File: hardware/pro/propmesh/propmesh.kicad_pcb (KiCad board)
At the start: 2 copper layers, 154 parts, among them CN1 LINE_OUT, J1 DC_IN, J10 SERVO, J11 SERVO, J12 SERVO, J13 SERVO, J15 MS_SEL, J16 DIAG_AUX, J19 MS_SEL, J2 DC_JACK, J20 MS_SEL, J21 MS_SEL, J22 MS_SEL, J23 MS_SEL, J24 DIAG_AUX, J3 RELAY_OUT, J4 TYPE-C-31-M-12, J5 SPEAKER, J6 RELAY_OUT, J7 SERVO, J8 RELAY_OUT, J9 SERVO, K1 HK4100F-DC5V-SHG, K2 HK4100F-DC5V-SHG, K3 HK4100F-DC5V-SHG, Q1 AO3400A, Q2 AOD4185, Q3 AO3400A, Q4 AO3400A, Q5 AO3400A, Q6 AO3400A, Q7 AO3400A, Q8 AO3400A, SW1 TS-1187A, SW2 TS-1187A, U1 TLV62569DBV, U2 AP64350SP-13, U3 ESP32-S3-WROOM-1U-N8R2, U4 USBLC6-2SC6, U5 PCA9685PW, U6 ULN2003A, U7 MAX98357AETE+T, U8 PCM5102APWR

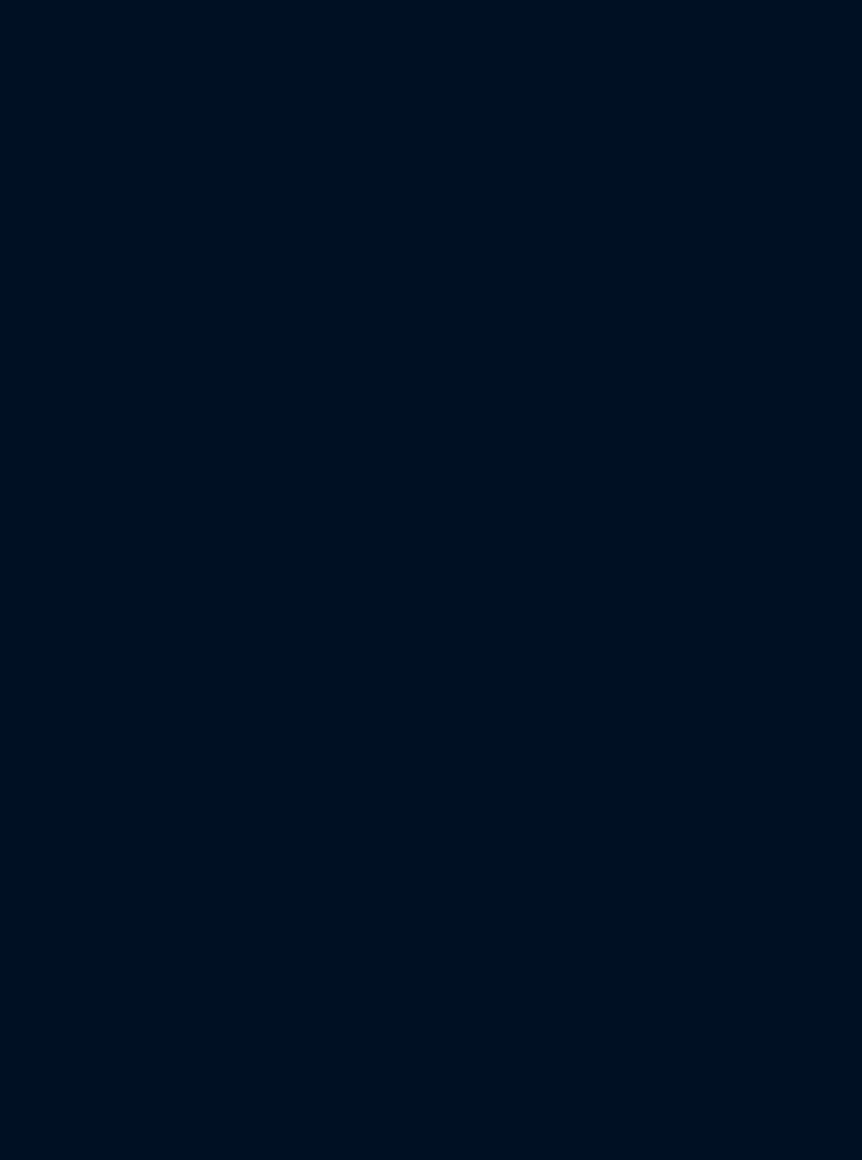
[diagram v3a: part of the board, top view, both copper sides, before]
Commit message: Sheet 07 (sensors + expansion) captured; sheet 05 spec ready
Sheet 07 drawn and verified: 3 clamped digital inputs (+ PIR header),
2 halved analog inputs, TSOP38238 on filtered 3V3, Qwiic (SH-1.0 clone
C7430446 — genuine JST stock-dead), 2x5 expansion header with GPIO45/46
strap protection. checknet all green, ERC clean bar the 4 LED labels
awaiting sheet 05. D2_MID global on motors + sensors sheets so
expansion pin 9 rides GPIO43's 1k.

Sheet 05 spec: AHCT125 moved to SOIC-14 C155176 (TSSOP dead at JLC),
strip 2 = 2x DG128-02P (04P dead), WS2812B-MINI-X2 status pixel
imported + datasheet-verified (pins, land pattern, VIH math).

Cost: all seven blocks now verified; parts subtotal $31.93,
duty-paid ~$48.55. Open item #2 mostly resolved (residual: JLC order
UI check before first PCBA run).

New repo rule after the C_A1 collision: spec refs are project-global —
never reuse one across sheet yamls (audio R_D3 -> R_DAT3, sensor caps
-> C_AN1/2).

Co-Authored-By: Claude Fable 5 <noreply@anthropic.com>
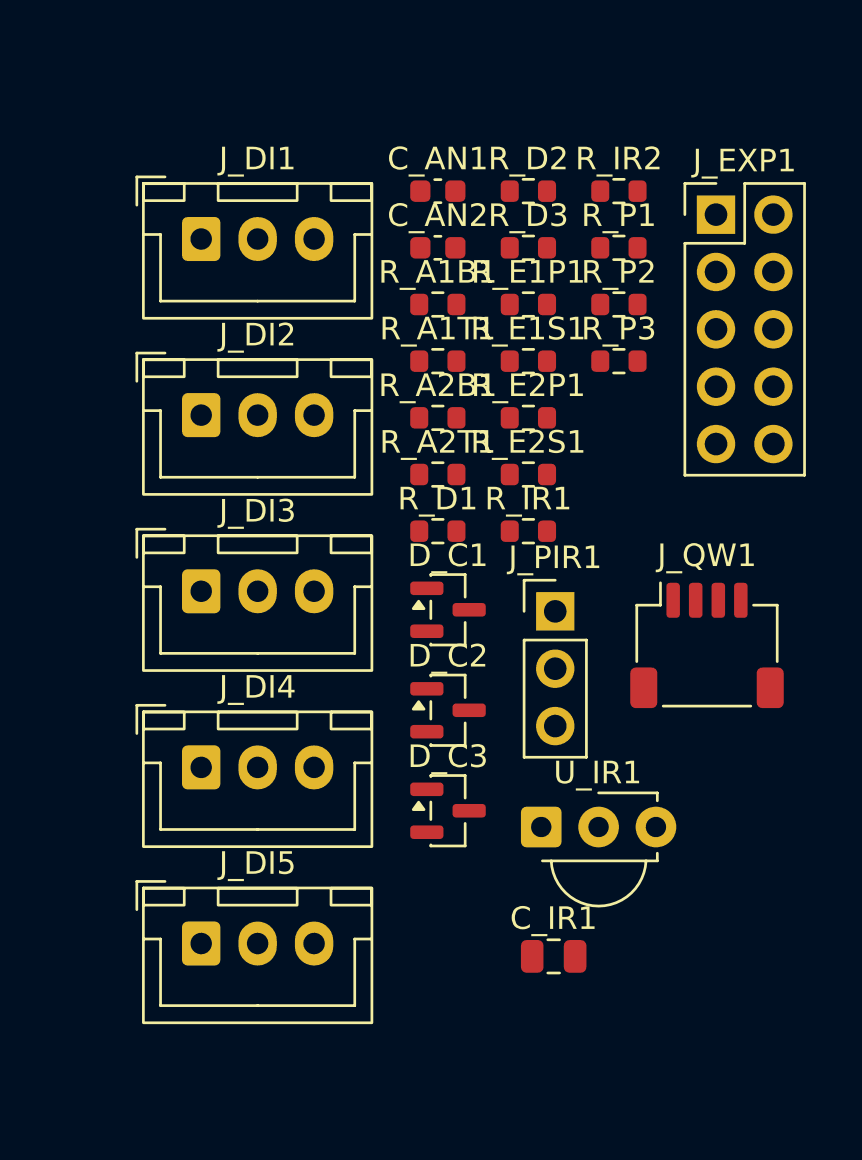
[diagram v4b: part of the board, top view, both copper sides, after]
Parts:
- added C_AN1: 100n, Capacitor_SMD:C_0603_1608Metric, F.Cu at (244.5, 23.8)
- added C_AN2: 100n, Capacitor_SMD:C_0603_1608Metric, F.Cu at (244.5, 26.3)
- added C_IR1: 10u, Capacitor_SMD:C_0805_2012Metric, F.Cu at (249.6, 57.6)
- added D_C1: BAT54S, Package_TO_SOT_SMD:SOT-23, F.Cu at (244.9, 42.3)
- added D_C2: BAT54S, Package_TO_SOT_SMD:SOT-23, F.Cu at (244.9, 46.7)
- added D_C3: BAT54S, Package_TO_SOT_SMD:SOT-23, F.Cu at (244.9, 51.2)
- added J_DI1: DIG_IN, Connector_JST:JST_XH_B3B-XH-A_1x03_P2.50mm_Vertical, F.Cu at (234.0, 25.9)
- added J_DI2: DIG_IN, Connector_JST:JST_XH_B3B-XH-A_1x03_P2.50mm_Vertical, F.Cu at (234.0, 33.7)
- added J_DI3: DIG_IN, Connector_JST:JST_XH_B3B-XH-A_1x03_P2.50mm_Vertical, F.Cu at (234.0, 41.5)
- added J_DI4: ANA_IN, Connector_JST:JST_XH_B3B-XH-A_1x03_P2.50mm_Vertical, F.Cu at (234.0, 49.3)
- added J_DI5: ANA_IN, Connector_JST:JST_XH_B3B-XH-A_1x03_P2.50mm_Vertical, F.Cu at (234.0, 57.1)
- added J_EXP1: EXPANSION, Connector_PinHeader_2.54mm:PinHeader_2x05_P2.54mm_Vertical, F.Cu at (256.8, 24.8)
- added J_PIR1: PIR_HDR, Connector_PinHeader_2.54mm:PinHeader_1x03_P2.54mm_Vertical, F.Cu at (249.7, 42.4)
- added J_QW1: QWIIC, Connector_JST:JST_SH_SM04B-SRSS-TB_1x04-1MP_P1.00mm_Horizontal, F.Cu at (256.4, 43.9)
- added R_A1B1: 100k, Resistor_SMD:R_0603_1608Metric, F.Cu at (244.5, 28.8)
- added R_A1T1: 100k, Resistor_SMD:R_0603_1608Metric, F.Cu at (244.5, 31.3)
- added R_A2B1: 100k, Resistor_SMD:R_0603_1608Metric, F.Cu at (244.5, 33.8)
- added R_A2T1: 100k, Resistor_SMD:R_0603_1608Metric, F.Cu at (244.5, 36.3)
- added R_D1: 1k, Resistor_SMD:R_0603_1608Metric, F.Cu at (244.5, 38.8)
- added R_D2: 1k, Resistor_SMD:R_0603_1608Metric, F.Cu at (248.5, 23.8)
- added R_D3: 1k, Resistor_SMD:R_0603_1608Metric, F.Cu at (248.5, 26.3)
- added R_E1P1: 10k, Resistor_SMD:R_0603_1608Metric, F.Cu at (248.5, 28.8)
- added R_E1S1: 100R, Resistor_SMD:R_0603_1608Metric, F.Cu at (248.5, 31.3)
- added R_E2P1: 10k, Resistor_SMD:R_0603_1608Metric, F.Cu at (248.5, 33.8)
- added R_E2S1: 100R, Resistor_SMD:R_0603_1608Metric, F.Cu at (248.5, 36.3)
- added R_IR1: 100, Resistor_SMD:R_0603_1608Metric, F.Cu at (248.5, 38.8)
- added R_IR2: 10k, Resistor_SMD:R_0603_1608Metric, F.Cu at (252.5, 23.8)
- added R_P1: 10k, Resistor_SMD:R_0603_1608Metric, F.Cu at (252.5, 26.3)
- added R_P2: 10k, Resistor_SMD:R_0603_1608Metric, F.Cu at (252.5, 28.8)
- added R_P3: 10k, Resistor_SMD:R_0603_1608Metric, F.Cu at (252.5, 31.3)
- added U_IR1: TSOP38238, OptoDevice:Vishay_MINICAST-3Pin, F.Cu at (249.0, 51.9)
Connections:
- net /Motors/D2_MID renamed D2_MID

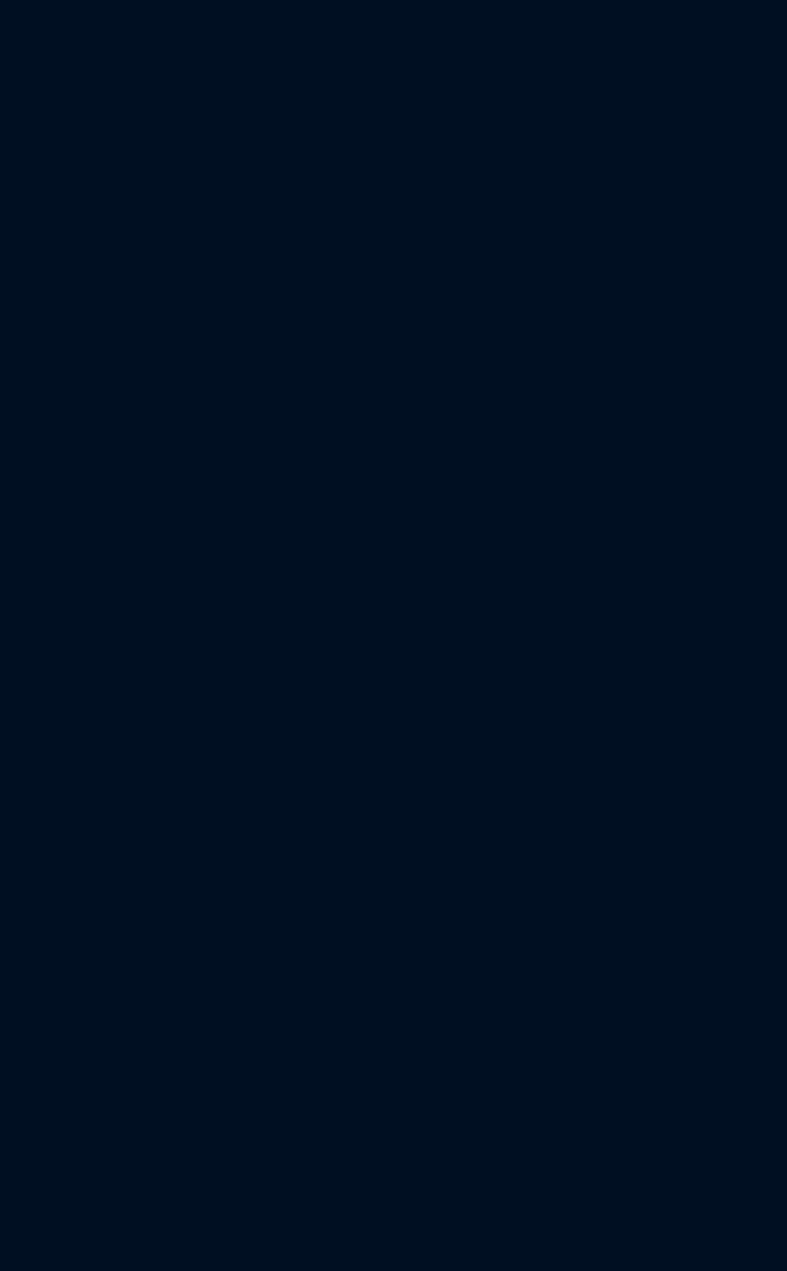
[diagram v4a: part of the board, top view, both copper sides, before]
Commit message: Pro schematic complete; enclosure, layout guide, timeline and radio decisions
Schematic: all seven design sheets drawn and green; project-wide ERC at
zero. IR receiver dropped (hidden board can't see a remote — plug-in on
a DIGITAL_IN); GPIO 3 became LED_STRIP_1_CLK; both strip outputs 3- or
4-wire through one octal SN74AHCT541DWR (three revisions of the shifter
in one day, no mode jumpers). Input FET symbol replaced: KiCad 10's
Device:Q_PMOS numbers pins D/G/S and matches no pad — the part would
have been unconnected with no ERC/DRC complaint. All 196 references
renumbered to standard sequential designators (yaml keeps spec names;
the checker prints both). Sheet 08 (test points) and the sheet 01
staged-power link headers specified per spec §2.6 — sheet 01's checker
is red until they are drawn.

checknet.py: symbol pins ⊆ footprint pads check (the silent killer),
multi-unit pin keys + per-unit diagrams (`units:`), symbol-vote sheet
anchoring for half-drawn sheets, orientation-aware net voting, foreign
part reporting, cross-sheet extras no longer crash the report.

Docs: hardware/pro/layout.md — placement by designator, IPC-2221 trace
widths, thermal, silk, ⚠ list, KiCad primer; every chip's datasheet
layout section read (WROOM-1U has NO keep-out; DRV8871 wants a bottom
GND pour; MAX98357A output-trace numbers). Enclosure plan (spec §2.3):
Multilink RNI-1500 / RNI-300, DRiBOX Medium, Joinfworld clear-lid box,
icotek KEL-DPZ entry plate, fit rule 210×140×60 mm inside; PSU
defaults (§2.9) and the 10 A input-path note. Software plan: timeline
design (ramps native, live scrub v1, Cue.start_offset_ms in schema),
yard access (walk-up AP, WireGuard-in-firmware, BYO remote), WiFi-PHY
radio decision vs Zigbee/BLE/LoRa, console served-from-bridge budget,
USB stays in CDC/JTAG mode (no auto-program transistors needed).

Co-Authored-By: Claude Fable 5.1 <noreply@anthropic.com>
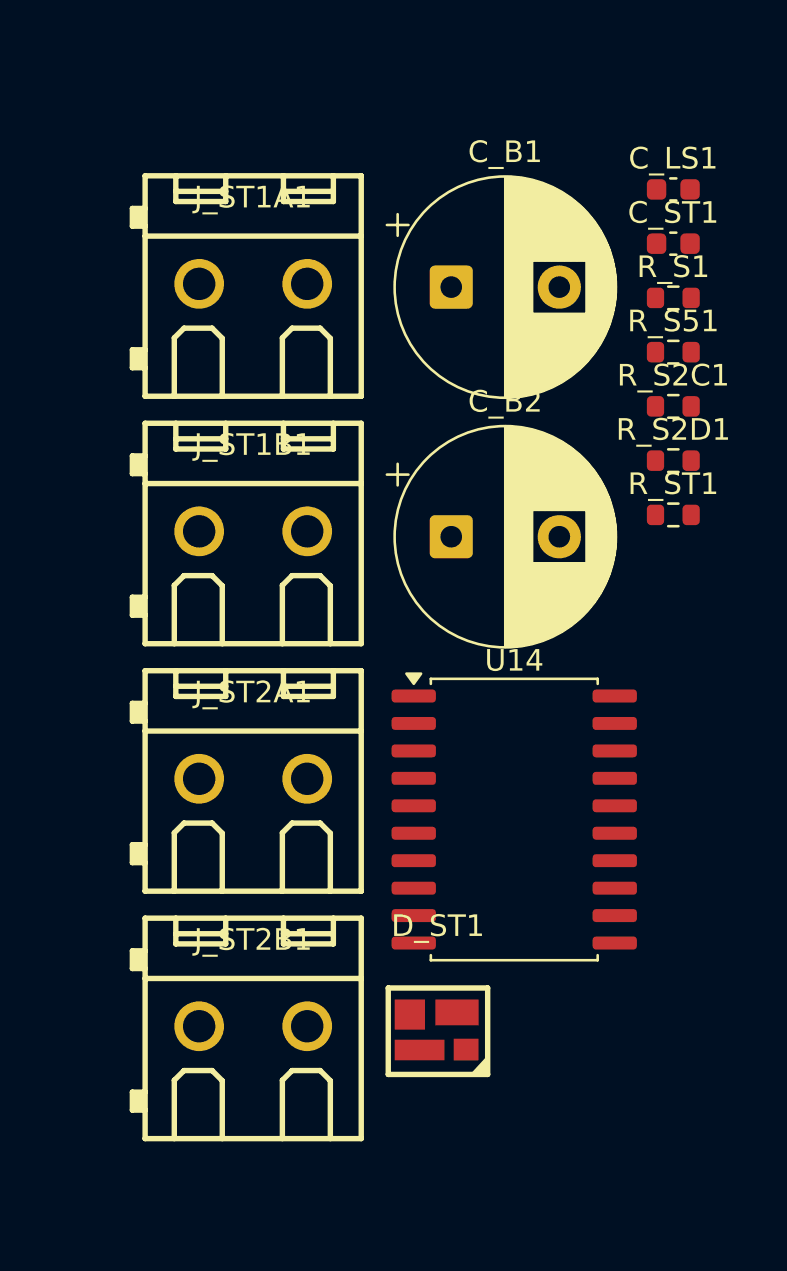
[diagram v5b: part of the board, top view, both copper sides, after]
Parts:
- added C_B1: 1000u/16V, Capacitor_THT:CP_Radial_D10.0mm_P5.00mm, F.Cu at (329.4, 66.3)
- added C_B2: 1000u/16V, Capacitor_THT:CP_Radial_D10.0mm_P5.00mm, F.Cu at (329.4, 77.8)
- added C_LS1: 100n, Capacitor_SMD:C_0603_1608Metric, F.Cu at (339.7, 61.8)
- added C_ST1: 100n, Capacitor_SMD:C_0603_1608Metric, F.Cu at (339.7, 64.3)
- added D_ST1: WS2812B-MINI, propmesh:LED-SMD_4P-L3.5-W3.5-TL_WS2812B-1, F.Cu at (328.8, 100.7)
- added J_ST1A1: LED1_PWR, propmesh:CONN-TH_DG128-5.0-02P-14-00A-H, F.Cu at (320.2, 66.1)
- added J_ST1B1: LED1_SIG, propmesh:CONN-TH_DG128-5.0-02P-14-00A-H, F.Cu at (320.2, 77.6)
- added J_ST2A1: LED2_PWR, propmesh:CONN-TH_DG128-5.0-02P-14-00A-H, F.Cu at (320.2, 89.0)
- added J_ST2B1: LED2_SIG, propmesh:CONN-TH_DG128-5.0-02P-14-00A-H, F.Cu at (320.2, 100.5)
- added R_S1: 330R, Resistor_SMD:R_0603_1608Metric, F.Cu at (339.7, 66.8)
- added R_S2C1: 330R, Resistor_SMD:R_0603_1608Metric, F.Cu at (339.7, 71.8)
- added R_S2D1: 330R, Resistor_SMD:R_0603_1608Metric, F.Cu at (339.7, 74.3)
- added R_S51: 330R, Resistor_SMD:R_0603_1608Metric, F.Cu at (339.7, 69.3)
- added R_ST1: 330R, Resistor_SMD:R_0603_1608Metric, F.Cu at (339.7, 76.8)
- added U14: SN74AHCT541, Package_SO:SOIC-20W_7.5x12.8mm_P1.27mm, F.Cu at (332.3, 90.9)
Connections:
- U3 pad 15: IR_RX -> LED_STRIP_1_CLK

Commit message: Sheet 08 (test points) + staged-power link headers; board synced 239/239
Sheet 08: 33 GPIO test points, 6 rail pads, DNP strap pad on GPIO 3 —
labels, values, wires and footprints generated from the yaml
(tools-side, not typed), power symbols cloned with every coordinate
shifted so texts travel with their parts. Sheet 01: JP_VIN / JP_5V /
JP_3V3 2-pin headers + shunts between input → 5 V buck → +5V rail →
+3V3 rail (spec §2.6 staged bring-up; a meter across a pulled shunt
reads that rail's current); PWR_FLAGs re-homed to the far side of each
jumper. Values use Colin's JP_* names; jumper pin numbering follows
the drawing.

All eight sheets green, ERC 0 violations, board updated with orphan
deletion: 239 footprints for 239 symbols, none differing.

checknet.py: extras from other sheets no longer crash the report or
the diagram renderer.

Co-Authored-By: Claude Fable 5.1 <noreply@anthropic.com>
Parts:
- removed C_IR1: 10u, Capacitor_SMD:C_0805_2012Metric
- removed the Q2 at (46.8, 70.1)
- removed R_IR1: 100, Resistor_SMD:R_0603_1608Metric
- removed R_IR2: 10k, Resistor_SMD:R_0603_1608Metric
- removed U_IR1: TSOP38238, OptoDevice:Vishay_MINICAST-3Pin
- added J48: JP_VIN, Connector_PinHeader_2.54mm:PinHeader_1x02_P2.54mm_Vertical, F.Cu at (377.8, 48.8)
- added J49: JP_5V, Connector_PinHeader_2.54mm:PinHeader_1x02_P2.54mm_Vertical, F.Cu at (382.4, 48.8)
- added J50: JP_3V3, Connector_PinHeader_2.54mm:PinHeader_1x02_P2.54mm_Vertical, F.Cu at (387.0, 48.8)
- added Q7: AOD4185, Package_TO_SOT_SMD:TO-252-2, F.Cu at (421.2, -54.8)
- added R53: DNP, Resistor_SMD:R_0603_1608Metric, F.Cu at (410.3, -57.7)
- added TP10: I2S_BCLK, TestPoint:TestPoint_Pad_1.5x1.5mm, F.Cu at (392.3, -32.4)
- added TP11: I2C_SDA, TestPoint:TestPoint_Pad_1.5x1.5mm, F.Cu at (395.8, -57.2)
- added TP12: I2C_SCL, TestPoint:TestPoint_Pad_1.5x1.5mm, F.Cu at (395.8, -53.7)
- added TP13: DIGITAL_IN_1, TestPoint:TestPoint_Pad_1.5x1.5mm, F.Cu at (395.8, -50.1)
- added TP14: DIGITAL_IN_2, TestPoint:TestPoint_Pad_1.5x1.5mm, F.Cu at (395.8, -46.6)
- added TP15: DIGITAL_IN_3, TestPoint:TestPoint_Pad_1.5x1.5mm, F.Cu at (395.8, -43.0)
- added TP16: STEPPER_1_STEP, TestPoint:TestPoint_Pad_1.5x1.5mm, F.Cu at (395.8, -39.5)
- added TP17: STEPPER_1_DIR, TestPoint:TestPoint_Pad_1.5x1.5mm, F.Cu at (395.8, -35.9)
- added TP18: I2S_LRCLK, TestPoint:TestPoint_Pad_1.5x1.5mm, F.Cu at (395.8, -32.4)
- added TP19: I2S_DOUT, TestPoint:TestPoint_Pad_1.5x1.5mm, F.Cu at (399.4, -57.2)
- added TP20: TMC_UART_TX, TestPoint:TestPoint_Pad_1.5x1.5mm, F.Cu at (399.4, -53.7)
- added TP21: TMC_UART_RX, TestPoint:TestPoint_Pad_1.5x1.5mm, F.Cu at (399.4, -50.1)
- added TP22: STEPPER_2_STEP, TestPoint:TestPoint_Pad_1.5x1.5mm, F.Cu at (399.4, -46.6)
- added TP23: MOTOR_B_IN1, TestPoint:TestPoint_Pad_1.5x1.5mm, F.Cu at (399.4, -43.0)
- added TP24: MOTOR_B_IN2, TestPoint:TestPoint_Pad_1.5x1.5mm, F.Cu at (399.4, -39.5)
- added TP25: STATUS_LED, TestPoint:TestPoint_Pad_1.5x1.5mm, F.Cu at (399.4, -35.9)
- added TP26: SD_CLK, TestPoint:TestPoint_Pad_1.5x1.5mm, F.Cu at (399.4, -32.4)
- added TP27: SD_CMD, TestPoint:TestPoint_Pad_1.5x1.5mm, F.Cu at (402.9, -57.2)
- added TP28: SD_D0, TestPoint:TestPoint_Pad_1.5x1.5mm, F.Cu at (402.9, -53.7)
- added TP29: STEPPER_1_DIAG, TestPoint:TestPoint_Pad_1.5x1.5mm, F.Cu at (402.9, -50.1)
- added TP3: BOOT_BUTTON, TestPoint:TestPoint_Pad_1.5x1.5mm, F.Cu at (392.3, -57.2)
- added TP30: STEPPER_2_DIAG, TestPoint:TestPoint_Pad_1.5x1.5mm, F.Cu at (402.9, -46.6)
- added TP31: MOTOR_A_IN1, TestPoint:TestPoint_Pad_1.5x1.5mm, F.Cu at (402.9, -43.0)
- added TP32: EXPANSION_1, TestPoint:TestPoint_Pad_1.5x1.5mm, F.Cu at (402.9, -39.5)
- added TP33: EXPANSION_2, TestPoint:TestPoint_Pad_1.5x1.5mm, F.Cu at (402.9, -35.9)
- added TP34: STEPPER_2_DIR, TestPoint:TestPoint_Pad_1.5x1.5mm, F.Cu at (402.9, -32.4)
- added TP35: MOTOR_A_IN2, TestPoint:TestPoint_Pad_1.5x1.5mm, F.Cu at (406.5, -57.2)
- added TP36: TP_VIN_RAW, TestPoint:TestPoint_Pad_1.5x1.5mm, F.Cu at (406.5, -53.7)
- added TP37: TP_VIN_PROT, TestPoint:TestPoint_Pad_1.5x1.5mm, F.Cu at (406.5, -50.1)
- added TP38: TP_5V, TestPoint:TestPoint_Pad_1.5x1.5mm, F.Cu at (406.5, -46.6)
- added TP39: TP_3V3, TestPoint:TestPoint_Pad_1.5x1.5mm, F.Cu at (406.5, -43.0)
- added TP4: ANALOG_IN_1, TestPoint:TestPoint_Pad_1.5x1.5mm, F.Cu at (392.3, -53.7)
- added TP40: TP_GND_A, TestPoint:TestPoint_Pad_1.5x1.5mm, F.Cu at (406.5, -39.5)
- added TP41: TP_GND_B, TestPoint:TestPoint_Pad_1.5x1.5mm, F.Cu at (406.5, -35.9)
- added TP5: ANALOG_IN_2, TestPoint:TestPoint_Pad_1.5x1.5mm, F.Cu at (392.3, -50.1)
- added TP6: LED_STRIP_1_CLK, TestPoint:TestPoint_Pad_1.5x1.5mm, F.Cu at (392.3, -46.6)
- added TP7: LED_STRIP_1_DATA, TestPoint:TestPoint_Pad_1.5x1.5mm, F.Cu at (392.3, -43.0)
- added TP8: LED_STRIP_2_DATA, TestPoint:TestPoint_Pad_1.5x1.5mm, F.Cu at (392.3, -39.5)
- added TP9: LED_STRIP_2_CLK, TestPoint:TestPoint_Pad_1.5x1.5mm, F.Cu at (392.3, -35.9)
- moved C24 301.9 mm to (334.7, 183.6)
- moved C26 301.9 mm to (334.7, 188.6)
- moved C27 301.9 mm to (334.7, 186.1)
- moved C30 301.9 mm to (334.7, 178.6)
- moved C31 301.9 mm to (334.7, 181.1)
- moved C32 301.9 mm to (334.7, 191.1)
- moved C33 301.9 mm to (334.7, 193.7)
- moved D2 301.9 mm to (540.2, 127.9)
- moved D3 301.9 mm to (540.2, 132.4)
- moved D4 301.9 mm to (540.2, 137.0)
- moved D5 301.9 mm to (540.2, 141.6)
- moved D6 301.9 mm to (540.2, 146.1)
- moved D7 301.9 mm to (540.2, 150.7)
- moved F1 301.9 mm to (329.0, 19.5)
- moved J21 301.9 mm to (422.4, 165.1)
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- renumbered C13 to C1, C12 to C10, C2 to C12, C5 to C13, C6 to C14, C1 to C15, C7 to C16, C8 to C17, C_BS1 to C18, C_BS2 to C19, C14 to C2, C_MA1 to C20, C_MA2 to C21, C_MB1 to C22, C_MB2 to C23, C20 to C24, C22 to C25, C23 to C26, C21 to C27, C_A1 to C28, C_A2 to C29, C15 to C3, C18 to C30, C19 to C31, C24 to C32, C25 to C33, C_DV1 to C34, C_DV2 to C35, C_AV1 to C36, C_AV2 to C37, C_CPV1 to C38, C_CPV2 to C39, C16 to C4, C_SD1 to C40, C_SD2 to C41, C_LS1 to C42, C_B1 to C43, C_ST1 to C44, C_B2 to C45, C_AN1 to C46, C_AN2 to C47, C17 to C5, C3 to C6, C9 to C7, C4 to C8, C10 to C9, D5 to D1, D3 to D10, D4 to D11, D_C1 to D12, D_C2 to D13, D_C3 to D14, D6 to D2, D7 to D3, D8 to D4, D9 to D5, D10 to D6, D11 to D7, D1 to D8, D2 to D9, J4 to J1, J_LED2 to J10, J_LED4 to J11, J_LED5 to J12, J_LED6 to J13, J3 to J14, J6 to J15, J8 to J16, J1 to J17, J2 to J18, J_S1L1 to J19, J7 to J2, J_S1R1 to J20, J16 to J21, J_S2R1 to J22, J_MA1 to J23, J_S2L1 to J24, XH1 to J25, J24 to J26, XH2 to J27, J_MB1 to J28, J21 to J29, J9 to J3, J15 to J30, J22 to J31, J19 to J32, J23 to J33, J20 to J34, J5 to J35, J_ST2B1 to J36, J_ST1B1 to J37, J_ST1A1 to J38, J_ST2A1 to J39, J10 to J4, J_DI4 to J40, J_DI1 to J41, J_EXP1 to J42, J_DI5 to J43, J_DI2 to J44, J_DI3 to J45, J_PIR1 to J46, J_QW1 to J47, J11 to J5, J13 to J6, J12 to J7, J_LED1 to J8, J_LED3 to J9, JP3 to JP2, D_ST1 to LED1, Q3 to Q2, Q4 to Q3, Q5 to Q4, Q6 to Q5, Q7 to Q6, R10 to R1, R17 to R10, R18 to R11, R19 to R12, R9 to R13, R1 to R14, R2 to R15, R8 to R16, R5 to R17, R3 to R18, R4 to R19, R11 to R2, R7 to R20, R6 to R21, R31 to R22, R29 to R23, R30 to R24, R_UTX1 to R25, R_ENP1 to R26, R22 to R27, R23 to R28, R24 to R29, R12 to R3, R25 to R30, R27 to R31, R28 to R32, R26 to R33, R_S51 to R34, R_S1 to R35, R_S2D1 to R36, R_S2C1 to R37, R_ST1 to R38, R_P1 to R39, R13 to R4, R_D1 to R40, R_A1B1 to R41, R_A1T1 to R42, R_E1S1 to R43, R_E2P1 to R44, R_E2S1 to R45, R_E1P1 to R46, R_D2 to R47, R_P2 to R48, R_A2B1 to R49, R20 to R5, R_A2T1 to R50, R_P3 to R51, R_D3 to R52, R21 to R6, R14 to R7, R15 to R8, R16 to R9, SW2 to SW1, SW1 to SW2, U4 to U1, U8 to U10, U14 to U11, U3 to U2, U6 to U3, U5 to U4, U2 to U5, U1 to U6, U_MA1 to U7, U_MB1 to U8, U7 to U9
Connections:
- C10 pad 1: +5V -> Net-(J49-Pin_2)
- C12 pad 1: VIN_PROT -> Net-(J48-Pin_2)
- C16 pad 1: +3V3 -> Net-(J50-Pin_2)
- C17 pad 1: +3V3 -> Net-(J50-Pin_2)
- C7 pad 1: VIN_PROT -> Net-(J48-Pin_2)
- C8 pad 1: +5V -> Net-(J49-Pin_2)
- C9 pad 1: +5V -> Net-(J49-Pin_2)
- L1 pad 2: +5V -> Net-(J49-Pin_2)
- L2 pad 2: +3V3 -> Net-(J50-Pin_2)
- R14 pad 1: +5V -> Net-(J49-Pin_2)
- R19 pad 1: +3V3 -> Net-(J50-Pin_2)
- U5 pad 2: VIN_PROT -> Net-(J48-Pin_2)
- U5 pad 3: VIN_PROT -> Net-(J48-Pin_2)
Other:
- board outline added: 130 x 100 mm
